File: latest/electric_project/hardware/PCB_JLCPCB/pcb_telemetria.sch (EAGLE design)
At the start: 43 parts

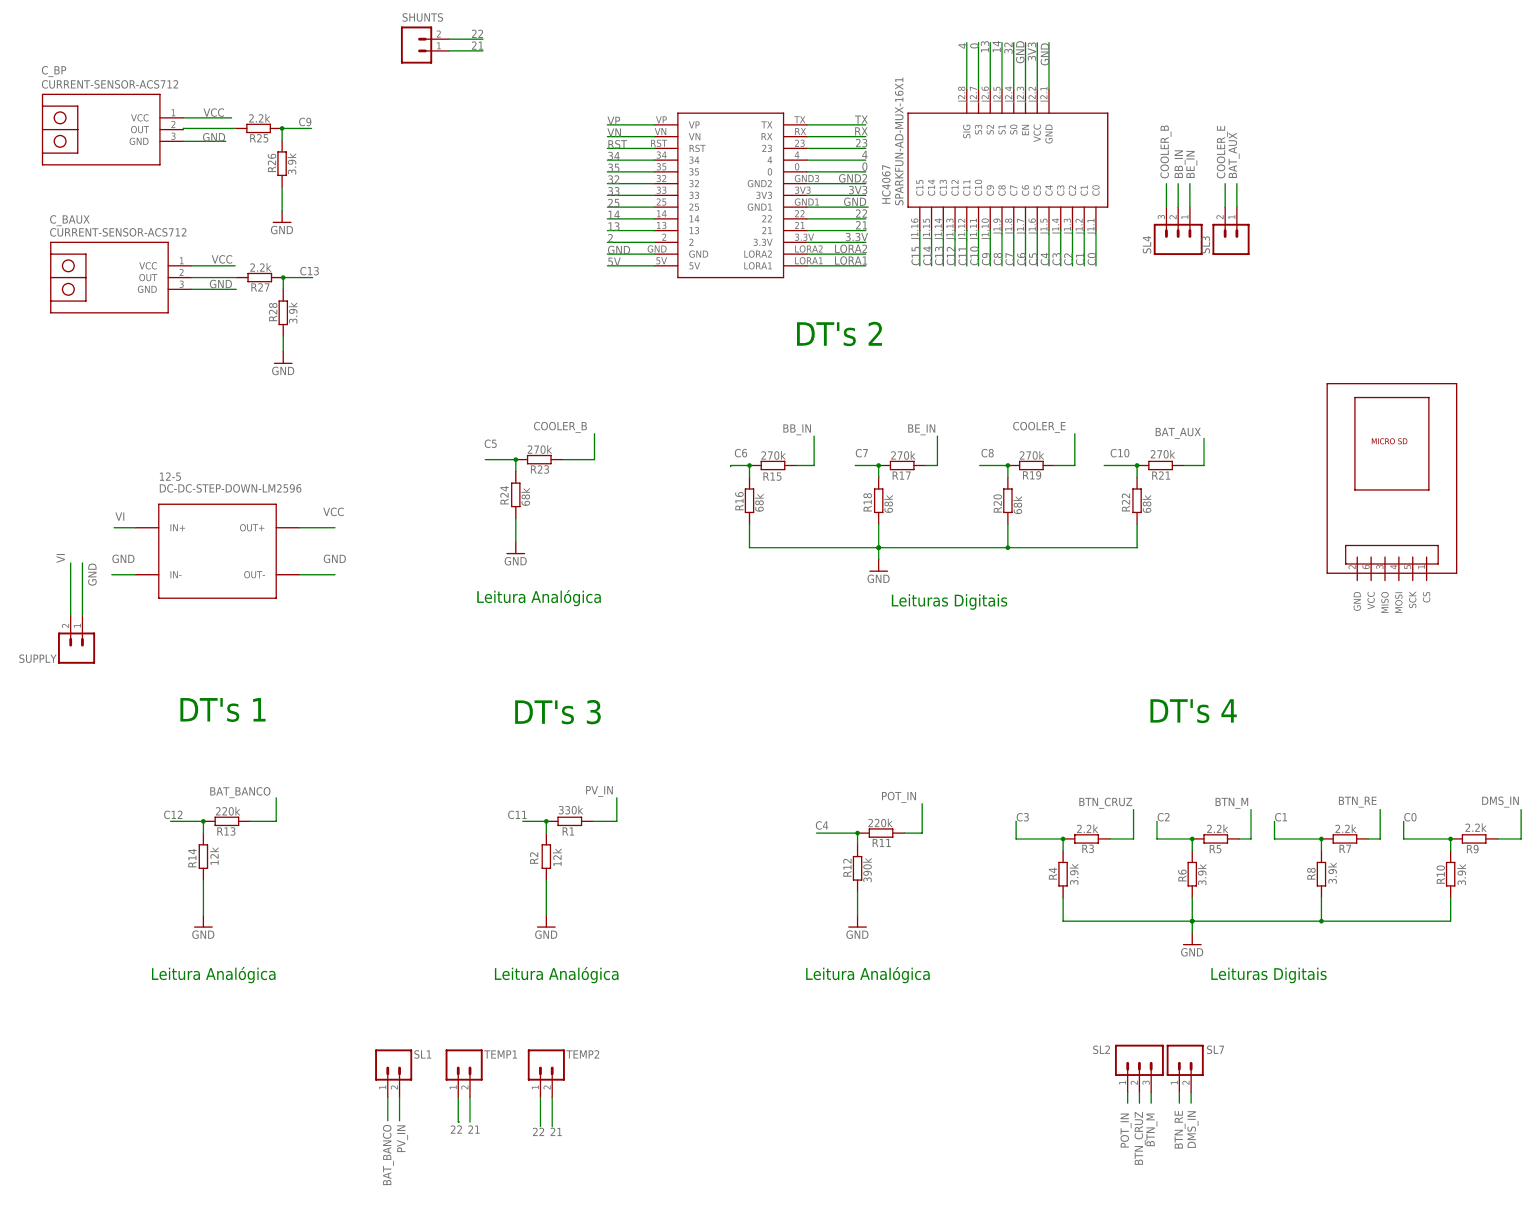
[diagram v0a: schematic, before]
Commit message: placa com trilhas finas e Mini-fit molex
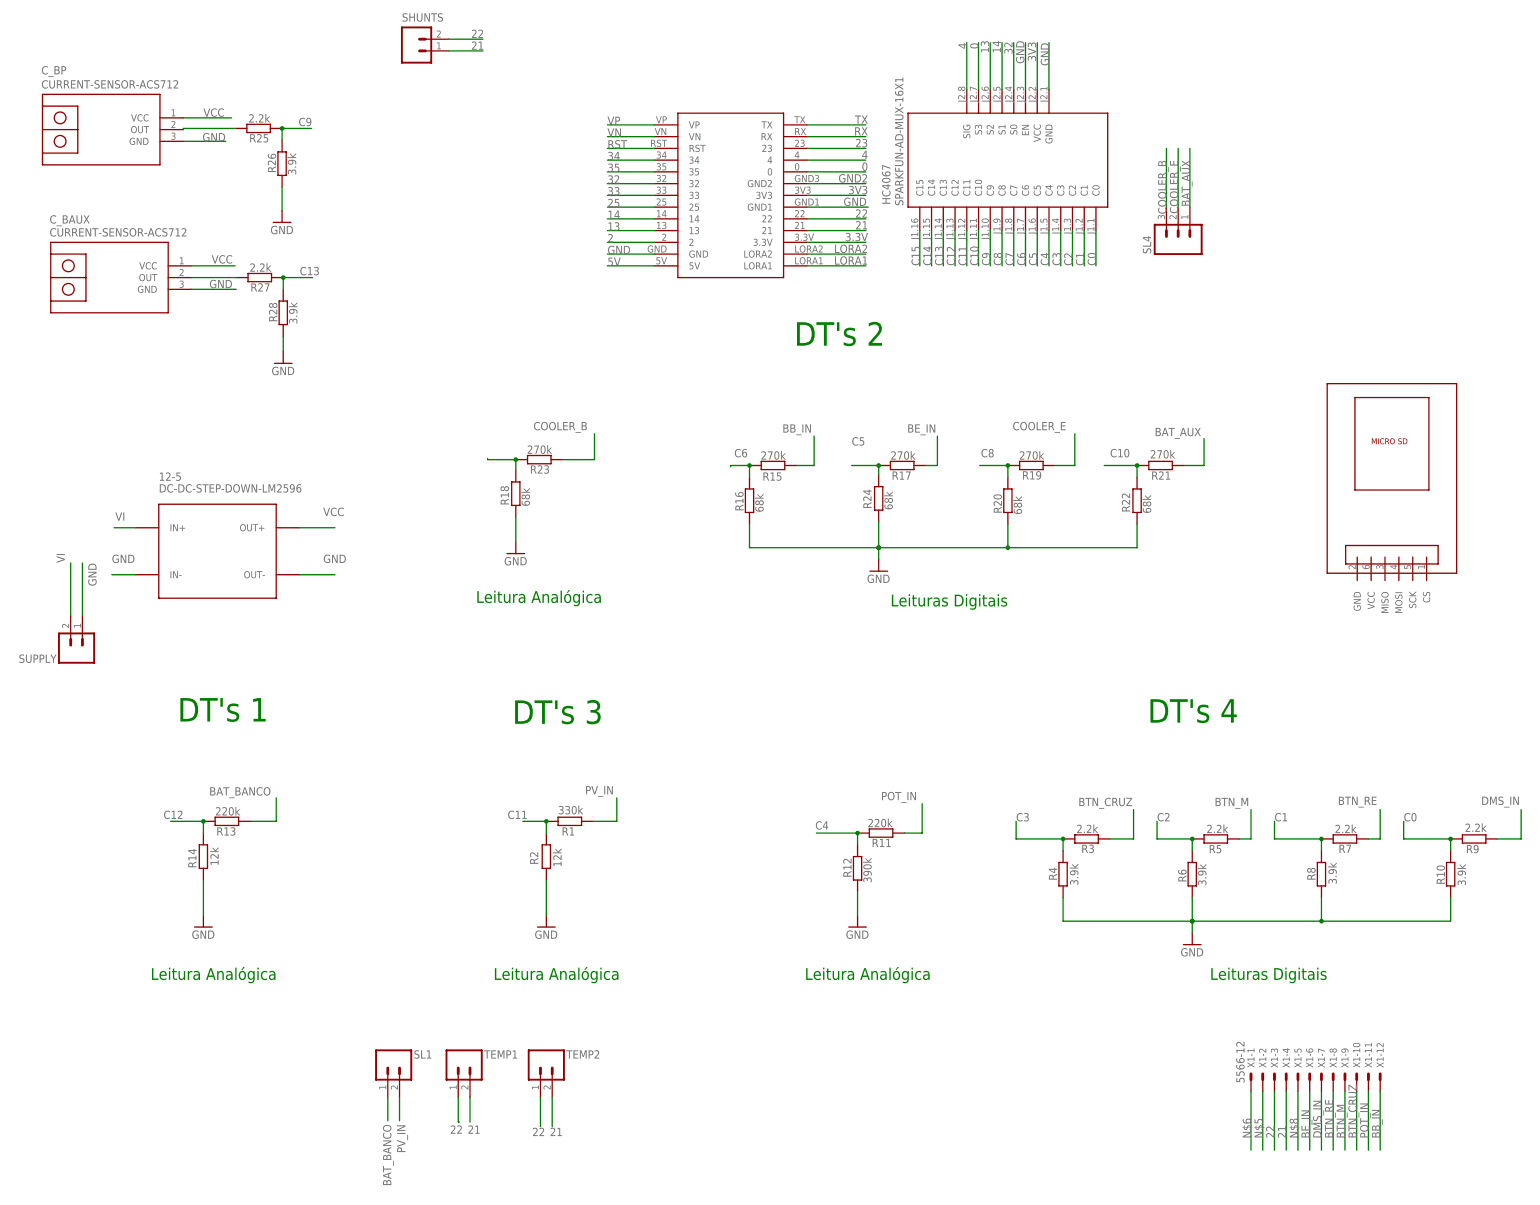
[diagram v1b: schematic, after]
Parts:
- removed SL2: (no value), con-amp-quick:M03
- removed SL3, SL7: (no value), con-amp-quick:M02
- added X1: 5566-12, con-molex:5566-12
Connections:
- new net GND3: R24.2
- new net N$5: X1-2.S
- new net N$6: X1-1.S
- new net N$8: X1-5.S
- net 21: now also X1-4.S
- net 22: now also X1-3.S
- net BAT_AUX: now also SL4.1; no longer SL3.1
- net BB_IN: now also X1-12.S; no longer SL4.2
- net BE_IN: now also X1-6.S; no longer SL4.1
- net BTN_CRUZ: now also X1-10.S; no longer SL2.2
- net BTN_M: now also X1-9.S; no longer SL2.3
- net BTN_RE: now also X1-8.S; no longer SL7.1
- net C5: now also R17.1; no longer R23.2
- net C7: now also R23.2; no longer R17.1
- net COOLER_E: now also SL4.2; no longer SL3.2
- net DMS_IN: now also X1-7.S; no longer SL7.2
- net GND: no longer R24.2
- net POT_IN: now also X1-11.S; no longer SL2.1
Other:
- moved on the sheet: R18, R24
